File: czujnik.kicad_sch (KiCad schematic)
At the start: 7 parts, among them J2 Conn_02x04, U3 BME280, U4 MB85RS256B

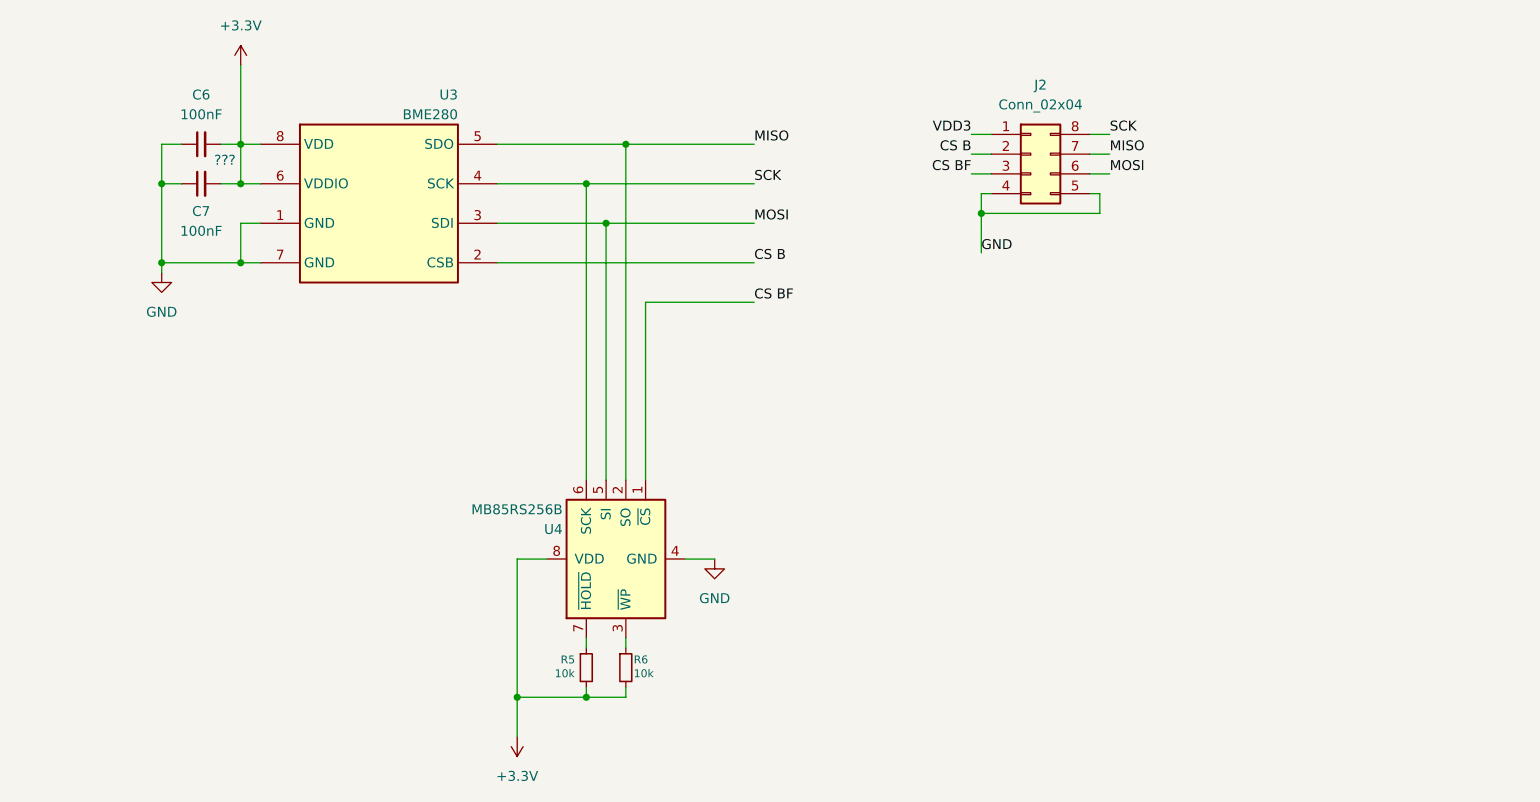
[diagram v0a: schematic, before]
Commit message: Pinout dla ESP32
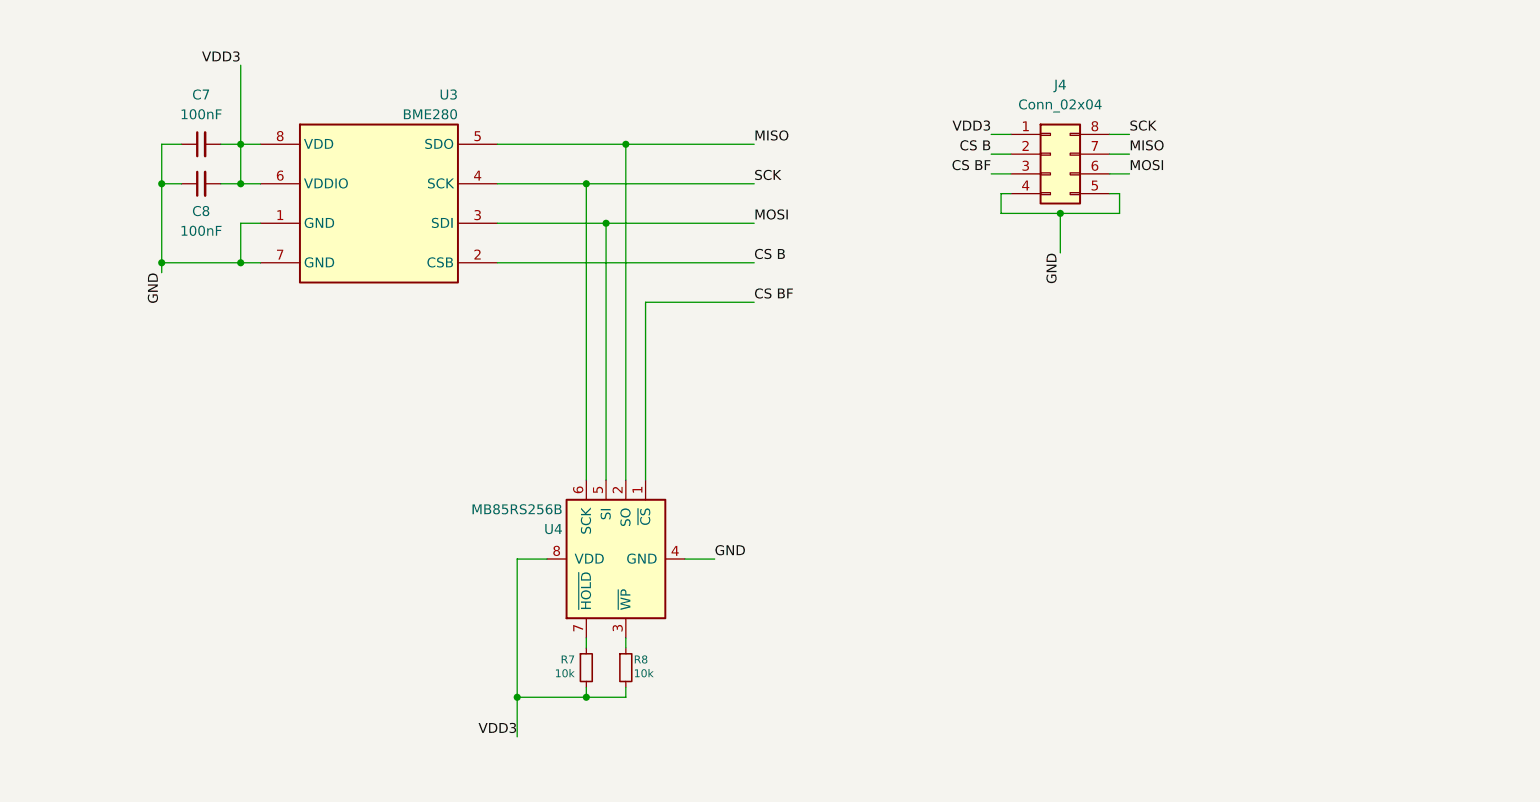
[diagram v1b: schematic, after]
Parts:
- renumbered C6 to C7, C7 to C8, J2 to J4, R5 to R7, R6 to R8
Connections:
- net +3.3V is gone; now on net VDD3: C7.2, C8.2, R7.2, R8.2, U3.6 (VDDIO), U3.8 (VDD), U4.8 (VDD)
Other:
- note removed: "???"
- moved on the sheet: J4

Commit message: wyswietlacz 1
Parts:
- removed R7: 10k, symbol Device:R_Small
- removed U4: MB85RS256B, symbol Memory_NVRAM:MB85RS256B
- added C9: 100nF, symbol Device:C_Small
- added R9: 10k, symbol Device:R_Small
- added U6: MB85RS256B, symbol Memory_NVRAM:MB85RS256B
- J6: renamed from J4; value Conn_02x04 -> Conn_C
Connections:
- net CS BF: now also U6.1 (~{CS})
- net GND: now also C9.1, U6.4 (GND)
- net MISO: now also U6.2 (SO)
- net MOSI: now also U6.5 (SI)
- net SCK: now also U6.6 (SCK)
- net VDD3: now also R8.1, C9.2, R9.1, U6.8 (VDD); no longer R8.2
- new net: R8.2, U6.7 (~{HOLD})
- new net: R9.2, U6.3 (~{WP})

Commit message: Orange 21.37
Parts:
- removed J6: Conn_C, symbol Connector_Generic:Conn_02x04_Counter_Clockwise
- added J4: Conn, symbol Connector_Generic:Conn_02x09_Odd_Even
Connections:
- net CS B: now also J4.3 (Pin_3)
- net CS BF: now also J4.5 (Pin_5)
- net GND: now also J4.17 (Pin_17), J4.18 (Pin_18)
- net MISO: now also J4.9 (Pin_9)
- net MOSI: now also J4.7 (Pin_7)
- net SCK: now also J4.11 (Pin_11)
- net VDD3: now also J4.1 (Pin_1)

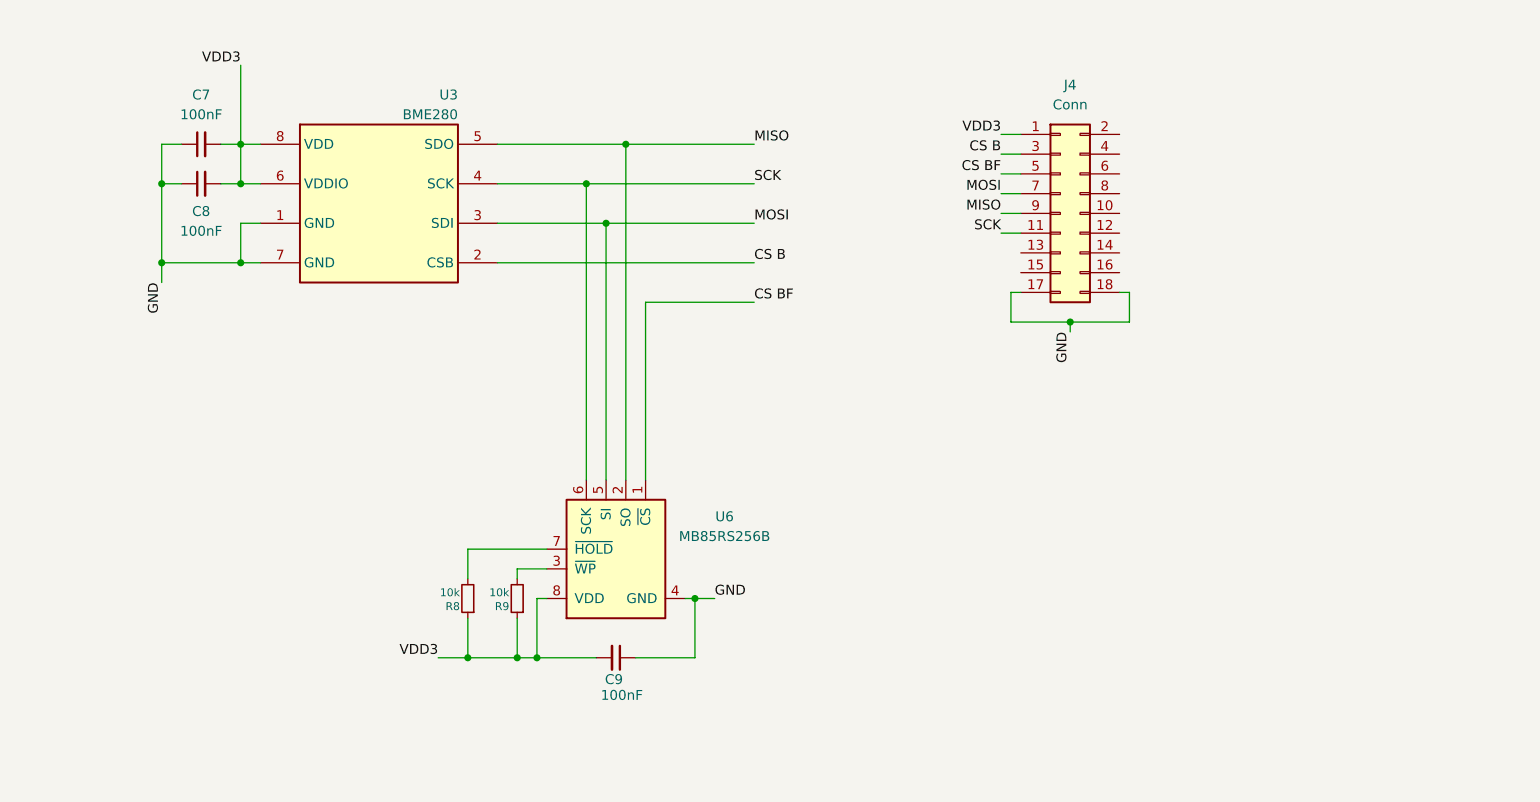
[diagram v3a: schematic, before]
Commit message: USB C update
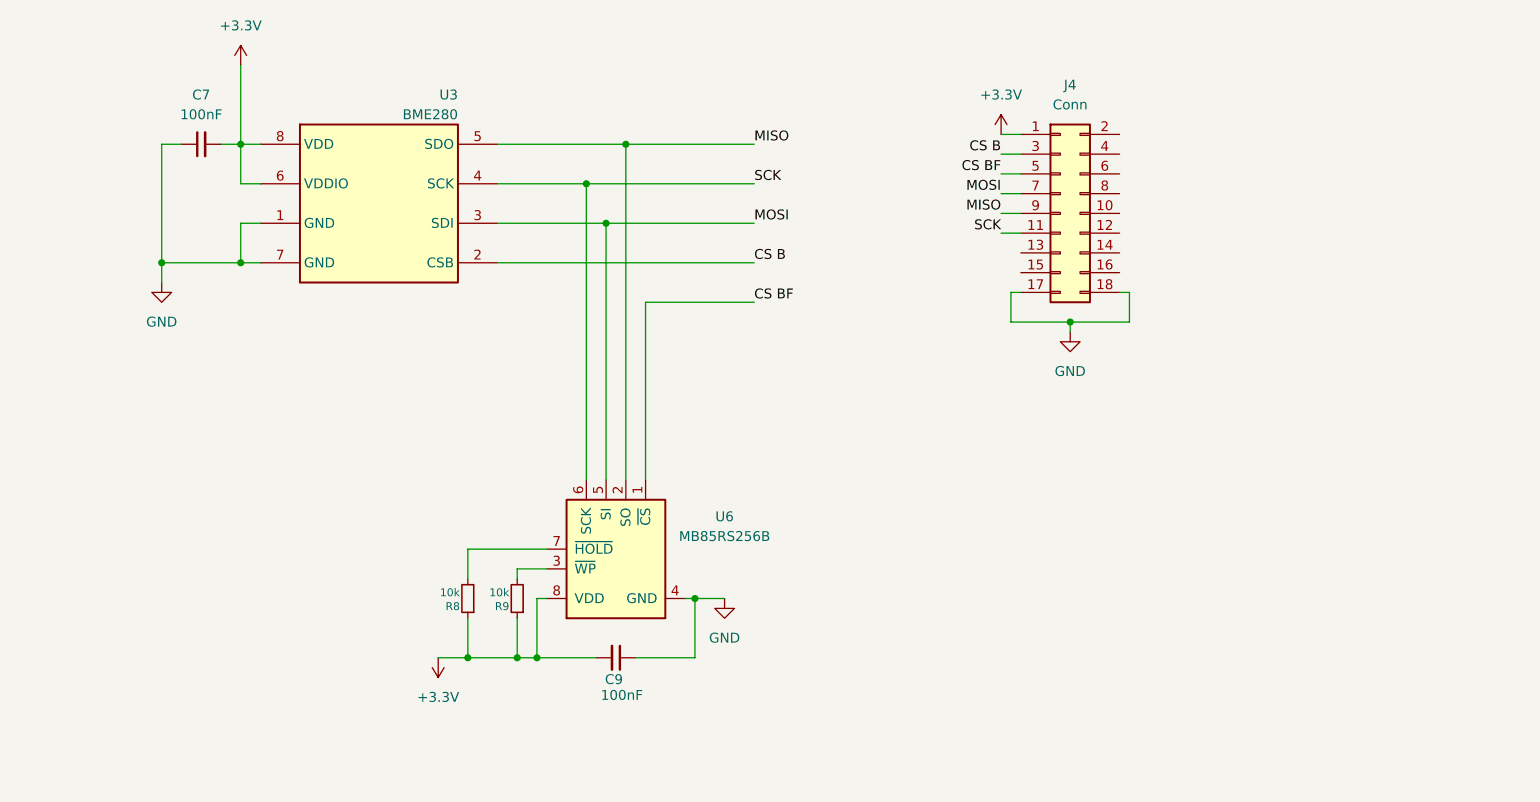
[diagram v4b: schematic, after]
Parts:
- removed C8: 100nF, symbol Device:C_Small
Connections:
- net VDD3 renamed +3.3V

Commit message: szczerze nie pamiętam co się tutaj zmieniło
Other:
- note added: "?A?EWr"
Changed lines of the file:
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@@
 	(generator_version "10.0")
 	(paper "A4")
+	(text "?A?EWr\n"
+		(exclude_from_sim no)
+		(at 67.564 71.374 0)
+		(effects
+			(font
+				(size 1.27 1.27)
+			)
+		)
+	)
 	(junction
 		(at 180.34 88.9)

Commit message: małe zmiany poprawki dsagolih
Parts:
- renumbered C7 to C8, R8 to R7, R9 to R8, U3 to U4, U6 to U5
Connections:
- no-connect marks 0 -> 10
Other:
- note removed: "?A?EWr"
- moved on the sheet: C8
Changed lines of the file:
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@@
 	(generator_version "10.0")
 	(paper "A4")
-	(text "?A?EWr\n"
-		(exclude_from_sim no)
-		(at 67.564 71.374 0)
-		(effects
-			(font
-				(size 1.27 1.27)
-			)
-		)
-	)
 	(junction
 		(at 180.34 88.9)
@@
 		(color 0 0 0 0)
 	)
+	(no_connect
+		(at 187.96 67.31)
+	)
+	(no_connect
+		(at 187.96 77.47)
+	)
+	(no_connect
+		(at 187.96 74.93)
+	)
+	(no_connect
+		(at 187.96 80.01)
+	)
+	(no_connect
+		(at 187.96 82.55)
+	)
+	(no_connect
+		(at 187.96 72.39)
+	)
+	(no_connect
+		(at 187.96 69.85)
+	)
+	(no_connect
+		(at 187.96 64.77)
+	)
+	(no_connect
+		(at 172.72 80.01)
+	)
+	(no_connect
+		(at 172.72 82.55)
+	)
 	(wire
 		(pts
@@
 	(wire
 		(pts
-			(xy 63.5 66.04) (xy 63.5 81.28)
-		)
-		(stroke
-			(width 0)
-			(type default)
-		)
-	)
-	(wire
-		(pts
 			(xy 111.76 124.46) (xy 113.03 124.46)
 		)
@@
 	(wire
 		(pts
+			(xy 172.72 80.01) (xy 173.99 80.01)
+		)
+		(stroke
+			(width 0)
+			(type default)
+		)
+	)
+	(wire
+		(pts
 			(xy 76.2 81.28) (xy 73.66 81.28)
 		)
@@
 	(wire
 		(pts
+			(xy 63.5 76.2) (xy 63.5 81.28)
+		)
+		(stroke
+			(width 0)
+			(type default)
+		)
+	)
+	(wire
+		(pts
 			(xy 173.99 64.77) (xy 171.45 64.77)
 		)
@@
 	(wire
 		(pts
+			(xy 172.72 82.55) (xy 173.99 82.55)
+		)
+		(stroke
+			(width 0)
+			(type default)
+		)
+	)
+	(wire
+		(pts
 			(xy 106.68 81.28) (xy 139.7 81.28)
 		)
@@
 	(wire
 		(pts
+			(xy 187.96 82.55) (xy 186.69 82.55)
+		)
+		(stroke
+			(width 0)
+			(type default)
+		)
+	)
+	(wire
+		(pts
 			(xy 106.68 76.2) (xy 120.65 76.2)
 		)
@@
 	(wire
 		(pts
+			(xy 187.96 69.85) (xy 186.69 69.85)
+		)
+		(stroke
+			(width 0)
+			(type default)
+		)
+	)
+	(wire
+		(pts
 			(xy 111.76 132.08) (xy 111.76 124.46)
 		)
@@
 	(wire
 		(pts
+			(xy 187.96 74.93) (xy 186.69 74.93)
+		)
+		(stroke
+			(width 0)
+			(type default)
+		)
+	)
+	(wire
+		(pts
 			(xy 120.65 76.2) (xy 139.7 76.2)
 		)
@@
 	(wire
 		(pts
+			(xy 187.96 67.31) (xy 186.69 67.31)
+		)
+		(stroke
+			(width 0)
+			(type default)
+		)
+	)
+	(wire
+		(pts
 			(xy 171.45 69.85) (xy 173.99 69.85)
 		)
@@
 	(wire
 		(pts
+			(xy 187.96 64.77) (xy 186.69 64.77)
+		)
+		(stroke
+			(width 0)
+			(type default)
+		)
+	)
+	(wire
+		(pts
 			(xy 73.66 81.28) (xy 63.5 81.28)
 		)
@@
 	(wire
 		(pts
-			(xy 71.12 66.04) (xy 73.66 66.04)
-		)
-		(stroke
-			(width 0)
-			(type default)
-		)
-	)
-	(wire
-		(pts
 			(xy 102.87 118.11) (xy 102.87 121.92)
 		)
@@
 	(wire
 		(pts
-			(xy 66.04 66.04) (xy 63.5 66.04)
+			(xy 187.96 77.47) (xy 186.69 77.47)
+		)
+		(stroke
+			(width 0)
+			(type default)
+		)
+	)
+	(wire
+		(pts
+			(xy 63.5 66.04) (xy 73.66 66.04)
 		)
 		(stroke
@@
 	(wire
 		(pts
+			(xy 63.5 66.04) (xy 63.5 71.12)
+		)
+		(stroke
+			(width 0)
+			(type default)
+		)
+	)
+	(wire
+		(pts
 			(xy 171.45 67.31) (xy 173.99 67.31)
 		)
@@
 	(wire
 		(pts
+			(xy 187.96 80.01) (xy 186.69 80.01)
+		)
+		(stroke
+			(width 0)
+			(type default)
+		)
+	)
+	(wire
+		(pts
 			(xy 132.08 132.08) (xy 132.08 124.46)
 		)
@@
 		(pts
 			(xy 123.19 66.04) (xy 123.19 109.22)
+		)
+		(stroke
+			(width 0)
+			(type default)
+		)
+	)
+	(wire
+		(pts
+			(xy 187.96 72.39) (xy 186.69 72.39)
 		)
 		(stroke
@@
 		(dnp no)
 		(fields_autoplaced yes)
-		(property "Reference" "#PWR06"
+		(property "Reference" "#PWR024"
 			(at 171.45 68.58 0)
 			(hide yes)
@@
 			(project "Projekt_smiw"
 				(path "/7e7ee3eb-03a8-4f9e-bb84-23570f6dcb78"
-					(reference "#PWR06")
+					(reference "#PWR024")
 					(unit 1)
 				)
@@
 		(dnp no)
 		(fields_autoplaced yes)
-		(property "Reference" "#PWR010"
+		(property "Reference" "#PWR020"
 			(at 63.5 90.17 0)
 			(hide yes)
@@
 			(project "Projekt_smiw"
 				(path "/7e7ee3eb-03a8-4f9e-bb84-23570f6dcb78"
-					(reference "#PWR010")
+					(reference "#PWR020")
 					(unit 1)
 				)
@@
 		(dnp no)
 		(fields_autoplaced yes)
-		(property "Reference" "#PWR08"
+		(property "Reference" "#PWR022"
 			(at 99.06 128.27 0)
 			(hide yes)
@@
 			(project "Projekt_smiw"
 				(path "/7e7ee3eb-03a8-4f9e-bb84-23570f6dcb78"
-					(reference "#PWR08")
+					(reference "#PWR022")
 					(unit 1)
 				)
@@
 		(in_pos_files yes)
 		(dnp no)
-		(property "Reference" "R8"
+		(property "Reference" "R7"
 			(at 101.854 125.476 0)
 			(show_name no)
@@
 			(project "Projekt_smiw"
 				(path "/7e7ee3eb-03a8-4f9e-bb84-23570f6dcb78"
-					(reference "R8")
+					(reference "R7")
 					(unit 1)
 				)
@@
 	(symbol
 		(lib_id "Device:C_Small")
-		(at 68.58 66.04 90)
+		(at 63.5 73.66 180)
 		(unit 1)
 		(body_style 1)
@@
 		(dnp no)
 		(fields_autoplaced yes)
-		(property "Reference" "C7"
-			(at 68.5863 59.69 90)
-			(show_name no)
-			(do_not_autoplace no)
-			(effects
-				(font
-					(size 1.27 1.27)
-				)
+		(property "Reference" "C8"
+			(at 66.04 72.3835 0)
+			(show_name no)
+			(do_not_autoplace no)
+			(effects
+				(font
+					(size 1.27 1.27)
+				)
+				(justify right)
 			)
 		)
 		(property "Value" "100nF"
-			(at 68.5863 62.23 90)
-			(show_name no)
-			(do_not_autoplace no)
-			(effects
-				(font
-					(size 1.27 1.27)
-				)
+			(at 66.04 74.9235 0)
+			(show_name no)
+			(do_not_autoplace no)
+			(effects
+				(font
+					(size 1.27 1.27)
+				)
+				(justify right)
 			)
 		)
 		(property "Footprint" ""
-			(at 68.58 66.04 0)
+			(at 63.5 73.66 0)
 			(hide yes)
 			(show_name no)
@@
 		)
 		(property "Datasheet" ""
-			(at 68.58 66.04 0)
+			(at 63.5 73.66 0)
 			(hide yes)
 			(show_name no)
@@
 		)
 		(property "Description" "Unpolarized capacitor, small symbol"
-			(at 68.58 66.04 0)
+			(at 63.5 73.66 0)
 			(hide yes)
 			(show_name no)
@@
 			(project "Projekt_smiw"
 				(path "/7e7ee3eb-03a8-4f9e-bb84-23570f6dcb78"
-					(reference "C7")
+					(reference "C8")
 					(unit 1)
 				)
@@
 		(dnp no)
 		(fields_autoplaced yes)
-		(property "Reference" "U6"
+		(property "Reference" "U5"
 			(at 135.89 113.9346 90)
 			(show_name no)
@@
 			(project "Projekt_smiw"
 				(path "/7e7ee3eb-03a8-4f9e-bb84-23570f6dcb78"
-					(reference "U6")
+					(reference "U5")
 					(unit 1)
 				)
@@
 		(dnp no)
 		(fields_autoplaced yes)
-		(property "Reference" "U3"
+		(property "Reference" "U4"
 			(at 101.6 59.69 0)
 			(show_name no)
@@
 			(project "Projekt_smiw"
 				(path "/7e7ee3eb-03a8-4f9e-bb84-23570f6dcb78"
-					(reference "U3")
+					(reference "U4")
 					(unit 1)
 				)
@@
 		(dnp no)
 		(fields_autoplaced yes)
-		(property "Reference" "#PWR07"
+		(property "Reference" "#PWR021"
 			(at 73.66 59.69 0)
 			(hide yes)
@@
 			(project "Projekt_smiw"
 				(path "/7e7ee3eb-03a8-4f9e-bb84-23570f6dcb78"
-					(reference "#PWR07")
+					(reference "#PWR021")
 					(unit 1)
 				)
@@
 		(dnp no)
 		(fields_autoplaced yes)
-		(property "Reference" "#PWR09"
+		(property "Reference" "#PWR025"
 			(at 180.34 96.52 0)
 			(hide yes)
@@
 			(project "Projekt_smiw"
 				(path "/7e7ee3eb-03a8-4f9e-bb84-23570f6dcb78"
-					(reference "#PWR09")
+					(reference "#PWR025")
 					(unit 1)
 				)
@@
 		(in_pos_files yes)
 		(dnp no)
-		(property "Reference" "R9"
+		(property "Reference" "R8"
 			(at 108.204 125.476 0)
 			(show_name no)
@@
 			(project "Projekt_smiw"
 				(path "/7e7ee3eb-03a8-4f9e-bb84-23570f6dcb78"
-					(reference "R9")
+					(reference "R8")
 					(unit 1)
 				)
@@
 		(dnp no)
 		(fields_autoplaced yes)
-		(property "Reference" "#PWR011"
+		(property "Reference" "#PWR023"
 			(at 135.89 130.81 0)
 			(hide yes)
@@
 			(project "Projekt_smiw"
 				(path "/7e7ee3eb-03a8-4f9e-bb84-23570f6dcb78"
-					(reference "#PWR011")
+					(reference "#PWR023")
 					(unit 1)
 				)

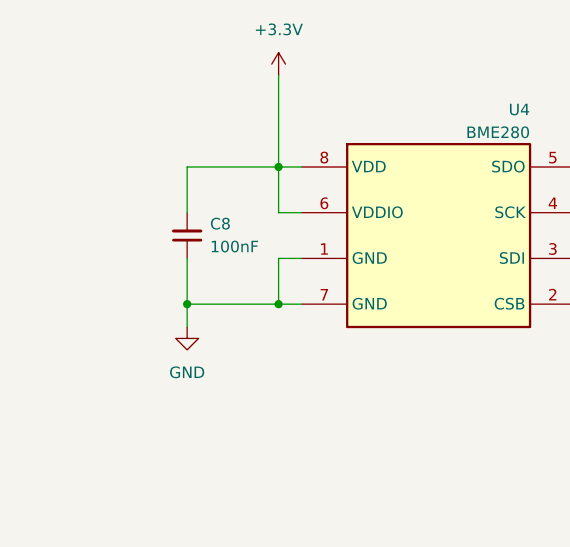
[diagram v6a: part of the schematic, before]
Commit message: dodano kondesnatory 100nF
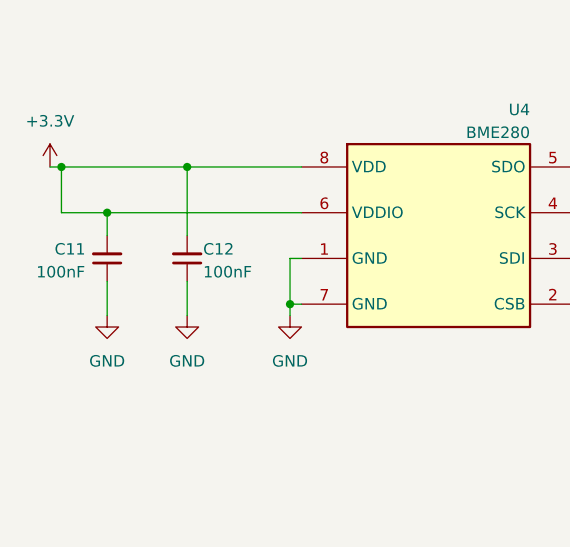
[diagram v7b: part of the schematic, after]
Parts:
- removed C8: 100nF, symbol Device:C_Small
- added C11, C12: 100nF, symbol Device:C_Small
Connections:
- net +3.3V: now also C11.2, C12.2
- net GND: now also C11.1, C12.1

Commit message: footprinty all, aheoi;rthipoawert;hiogsedho;i yay Halo? Schemat zrobiony ^^ pewnie nie
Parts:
- added J5: Conn OUT, Connector_PinSocket_2.54mm:PinSocket_2x09_P2.54mm_Vertical, symbol Connector_Generic:Conn_02x09_Odd_Even
- C12: renamed from C11; footprint (none) -> Capacitor_SMD:C_0603_1608Metric
- C13: renamed from C12; footprint (none) -> Capacitor_SMD:C_0603_1608Metric
- C14: renamed from C9; footprint (none) -> Capacitor_SMD:C_0603_1608Metric
- J4: value Conn -> Conn IN; footprint (none) -> Connector_PinHeader_2.54mm:PinHeader_2x09_P2.54mm_Vertical
- R6: renamed from R7; footprint (none) -> Resistor_SMD:R_0603_1608Metric
- R7: renamed from R8; footprint (none) -> Resistor_SMD:R_0603_1608Metric
- U5: footprint (none) -> Package_SO:SOIC-8_3.9x4.9mm_P1.27mm
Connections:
- net +3.3V: now also J5.1 (Pin_1)
- net GND: now also J5.17 (Pin_17), J5.18 (Pin_18)
- net MISO: now also J5.9 (Pin_9)
- net MOSI: now also J5.7 (Pin_7)
- net SCK: now also J5.11 (Pin_11)
- net ROW 1: now reaches J4.10 (Pin_10)
- net ROW 1: now also J5.10 (Pin_10)
- net ROW 2: now reaches J4.12 (Pin_12)
- net ROW 2: now also J5.12 (Pin_12)
- net SDA: now reaches J4.13 (Pin_13)
- net SDA: now also J5.13 (Pin_13)
- net ROW 3: now reaches J4.14 (Pin_14)
- net ROW 3: now also J5.14 (Pin_14)
- net SCL: now reaches J4.15 (Pin_15)
- net SCL: now also J5.15 (Pin_15)
- net ROW 4: now reaches J4.16 (Pin_16)
- net ROW 4: now also J5.16 (Pin_16)
- net COL 1: now reaches J4.2 (Pin_2)
- net COL 1: now also J5.2 (Pin_2)
- net COL 2: now reaches J4.4 (Pin_4)
- net COL 2: now also J5.4 (Pin_4)
- net COL 3: now reaches J4.6 (Pin_6)
- net COL 3: now also J5.6 (Pin_6)
- net COL 4: now reaches J4.8 (Pin_8)
- net COL 4: now also J5.8 (Pin_8)
- net CS B renamed CS BME280
- net CS BME280: now also J5.3 (Pin_3)
- net CS BF renamed CS FRAM SPI
- net CS FRAM SPI: now also J5.5 (Pin_5)
- no-connect marks 10 -> 0
